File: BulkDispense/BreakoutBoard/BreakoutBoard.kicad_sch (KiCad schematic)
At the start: 0 parts

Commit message: Most Recent Changes
Added New Connector Type (3M Mini-Clamp Series)
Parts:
- added J1: Bubble Sensor Power, PartsLibrary:CONN_37204-62A3-004PL_3MM, symbol Connector:Conn_01x04_Socket
- added J10: Reagent Media Valve Signal, PartsLibrary:CONN_37204-62A3-004PL_3MM, symbol Connector:Conn_01x04_Socket
- added J11: Proportional Control Valve, PartsLibrary:CONN_37204-62A3-004PL_3MM, symbol Connector:Conn_01x04_Socket
- added J12: Reagent Media Valve GND, PartsLibrary:CONN_37204-62A3-004PL_3MM, symbol Connector:Conn_01x04_Socket
- added J13: Pressure Sensor, PartsLibrary:CONN_37204-62A3-004PL_3MM, symbol Connector:Conn_01x04_Socket
- added J14: Waste 2/2 Media Valve GND, PartsLibrary:CONN04_2165712004_MOL, symbol Connector:Conn_01x04_Socket
- added J15: Waste 2/2 Media Valve Power, PartsLibrary:CONN04_2165712004_MOL, symbol Connector:Conn_01x04_Socket
- added J16: Waste 3/2 Media Valve, PartsLibrary:CONN04_2165712004_MOL, symbol Connector:Conn_01x04_Socket
- added J17: Waste Bottle Sensor 1, PartsLibrary:CONN03_2165711003_MOL, symbol Connector:Conn_01x03_Socket
- added J18: Waste Line Sensor 2, PartsLibrary:CONN03_2165711003_MOL, symbol Connector:Conn_01x03_Socket
- added J19: Waste Line Sensor 1, PartsLibrary:CONN03_2165711003_MOL, symbol Connector:Conn_01x03_Socket
- added J2: Bubble Sensor Signal, PartsLibrary:CONN_37204-62A3-004PL_3MM, symbol Connector:Conn_01x04_Socket
- added J20: Waste Bottle Sensor 2, PartsLibrary:CONN03_2165711003_MOL, symbol Connector:Conn_01x03_Socket
- added J21: Waste Vacuum Sensor 1, PartsLibrary:CONN03_2165711003_MOL, symbol Connector:Conn_01x03_Socket
- added J22: Waste Vacuum Sensor 2, PartsLibrary:CONN03_2165711003_MOL, symbol Connector:Conn_01x03_Socket
- added J23: MAXI Power, PartsLibrary:CONN02_2165711002_MOL, symbol Connector:Conn_01x02_Socket
- added J3: Bubble Sensor GND, PartsLibrary:CONN_37204-62A3-004PL_3MM, symbol Connector:Conn_01x04_Socket
- added J33: 37212-62M3-003PL, CONN_37212-62M3-003PL_3MM, symbol 37212-62M3-003PL:37212-62M3-003PL
- added J4: Overflow Sensor Power, PartsLibrary:CONN_37204-62A3-004PL_3MM, symbol Connector:Conn_01x04_Socket
- added J5: Overflow Sensor GND, PartsLibrary:CONN_37204-62A3-004PL_3MM, symbol Connector:Conn_01x04_Socket
- added J6: Overflow Sensor Signal, PartsLibrary:CONN_37204-62A3-004PL_3MM, symbol Connector:Conn_01x04_Socket
- added J7: Power Source, PartsLibrary:691137710002, symbol Connector:Screw_Terminal_01x02
- added J8: Reagent Valve Power, PartsLibrary:CONN_37204-62A3-004PL_3MM, symbol Connector:Conn_01x04_Socket
- added J9: Reagent Valve GND, PartsLibrary:CONN_37204-62A3-004PL_3MM, symbol Connector:Conn_01x04_Socket
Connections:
- new net +24V: J1.1 (Pin_1), J1.2 (Pin_2), J1.3 (Pin_3), J1.4 (Pin_4), J11.1 (Pin_1), J13.1 (Pin_1), J15.1 (Pin_1), J15.2 (Pin_2), J15.3 (Pin_3), J15.4 (Pin_4), J16.1 (Pin_1), J16.2 (Pin_2), J17.1 (Pin_1), J18.1 (Pin_1), J19.1 (Pin_1), J20.1 (Pin_1), J21.1 (Pin_1), J22.1 (Pin_1), J23.1 (Pin_1), J33.1, J33.4, J4.1 (Pin_1), J4.2 (Pin_2), J4.3 (Pin_3), J4.4 (Pin_4), J7.1 (Pin_1), J8.1 (Pin_1), J8.2 (Pin_2), J8.3 (Pin_3), J8.4 (Pin_4)
- new net AI0: J2.4 (Pin_4)
- new net AI1: J2.3 (Pin_3)
- new net AI12: J13.4 (Pin_4)
- new net AI13: J11.2 (Pin_2)
- new net AI2: J2.2 (Pin_2)
- new net AI3: J2.1 (Pin_1)
- new net AI4: J19.3 (Pin_3), J33.3
- new net AI5: J18.3 (Pin_3), J33.5
- new net AI6: J20.3 (Pin_3), J33.6
- new net AI7: J17.3 (Pin_3), J33.7
- new net AI8: J21.3 (Pin_3), J33.8
- new net AI9: J22.3 (Pin_3), J33.9
- new net AO0: J11.3 (Pin_3)
- new net DI0: J6.4 (Pin_4)
- new net DI1: J6.3 (Pin_3)
- new net DI2: J6.2 (Pin_2)
- new net DI3: J6.1 (Pin_1)
- new net DO0: J10.4 (Pin_4)
- new net DO1: J10.3 (Pin_3)
- new net DO2: J10.2 (Pin_2)
- new net DO3: J10.1 (Pin_1)
- new net GND: J11.4 (Pin_4), J12.1 (Pin_1), J12.2 (Pin_2), J12.3 (Pin_3), J12.4 (Pin_4), J13.2 (Pin_2), J13.3 (Pin_3), J14.1 (Pin_1), J14.2 (Pin_2), J14.3 (Pin_3), J14.4 (Pin_4), J16.3 (Pin_3), J16.4 (Pin_4), J17.2 (Pin_2), J18.2 (Pin_2), J19.2 (Pin_2), J20.2 (Pin_2), J21.2 (Pin_2), J22.2 (Pin_2), J23.2 (Pin_2), J3.1 (Pin_1), J3.2 (Pin_2), J3.3 (Pin_3), J3.4 (Pin_4), J33.12, J33.2, J5.1 (Pin_1), J5.2 (Pin_2), J5.3 (Pin_3), J5.4 (Pin_4), J7.2 (Pin_2), J9.1 (Pin_1), J9.2 (Pin_2), J9.3 (Pin_3), J9.4 (Pin_4)
- no-connect marks 0 -> 2
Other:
- added sheet Controllino MAXI Expansion Board (expansion_board.kicad_sch)
- note added: "BS1"
- note added: "BS2"
- note added: "BS3"
- note added: "BS4"
- note added: "Dispense"
- note added: "MV1"
- note added: "MV2"
- note added: "MV3"
- note added: "MV4"
- note added: "OS1"
- note added: "OS2"
- note added: "OS3"
- note added: "OS4"
- note added: "Pheonix Contact"
- note added: "Power Source"
- note added: "R0"
- note added: "R1"
- note added: "R2"
- note added: "R3"
- note added: "R4"
- note added: "R5"
- note added: "R6"
- note added: "R7"
- note added: "R8"
- note added: "R9"
- note added: "Waste"

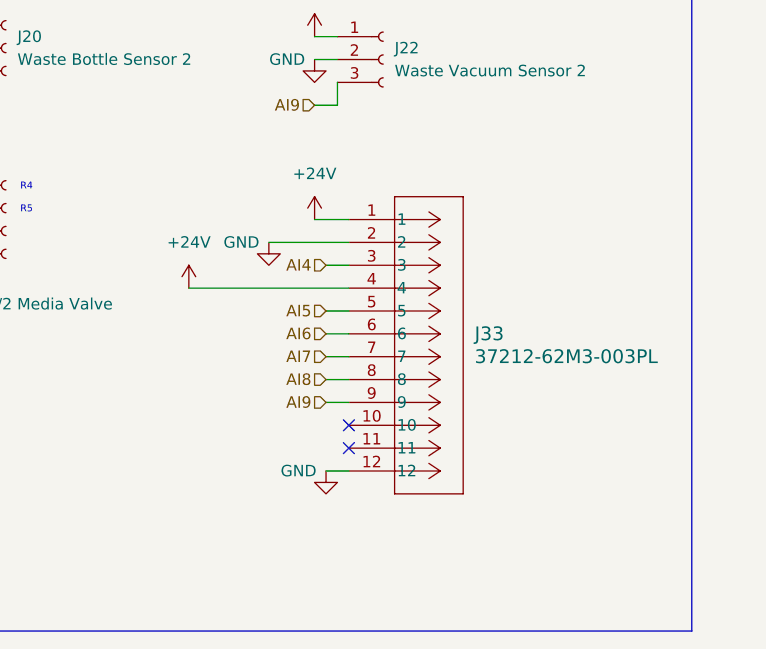
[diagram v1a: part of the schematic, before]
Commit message: Update 3POS Connectors with Mini-Clamp
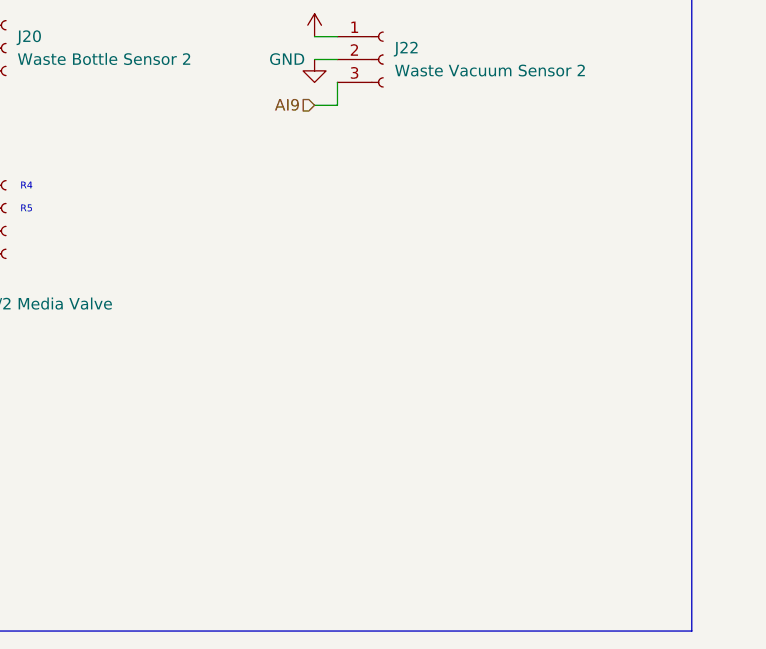
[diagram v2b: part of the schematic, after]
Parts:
- removed J33: 37212-62M3-003PL, CONN_37212-62M3-003PL_3MM, symbol 37212-62M3-003PL:37212-62M3-003PL
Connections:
- no-connect marks 2 -> 0

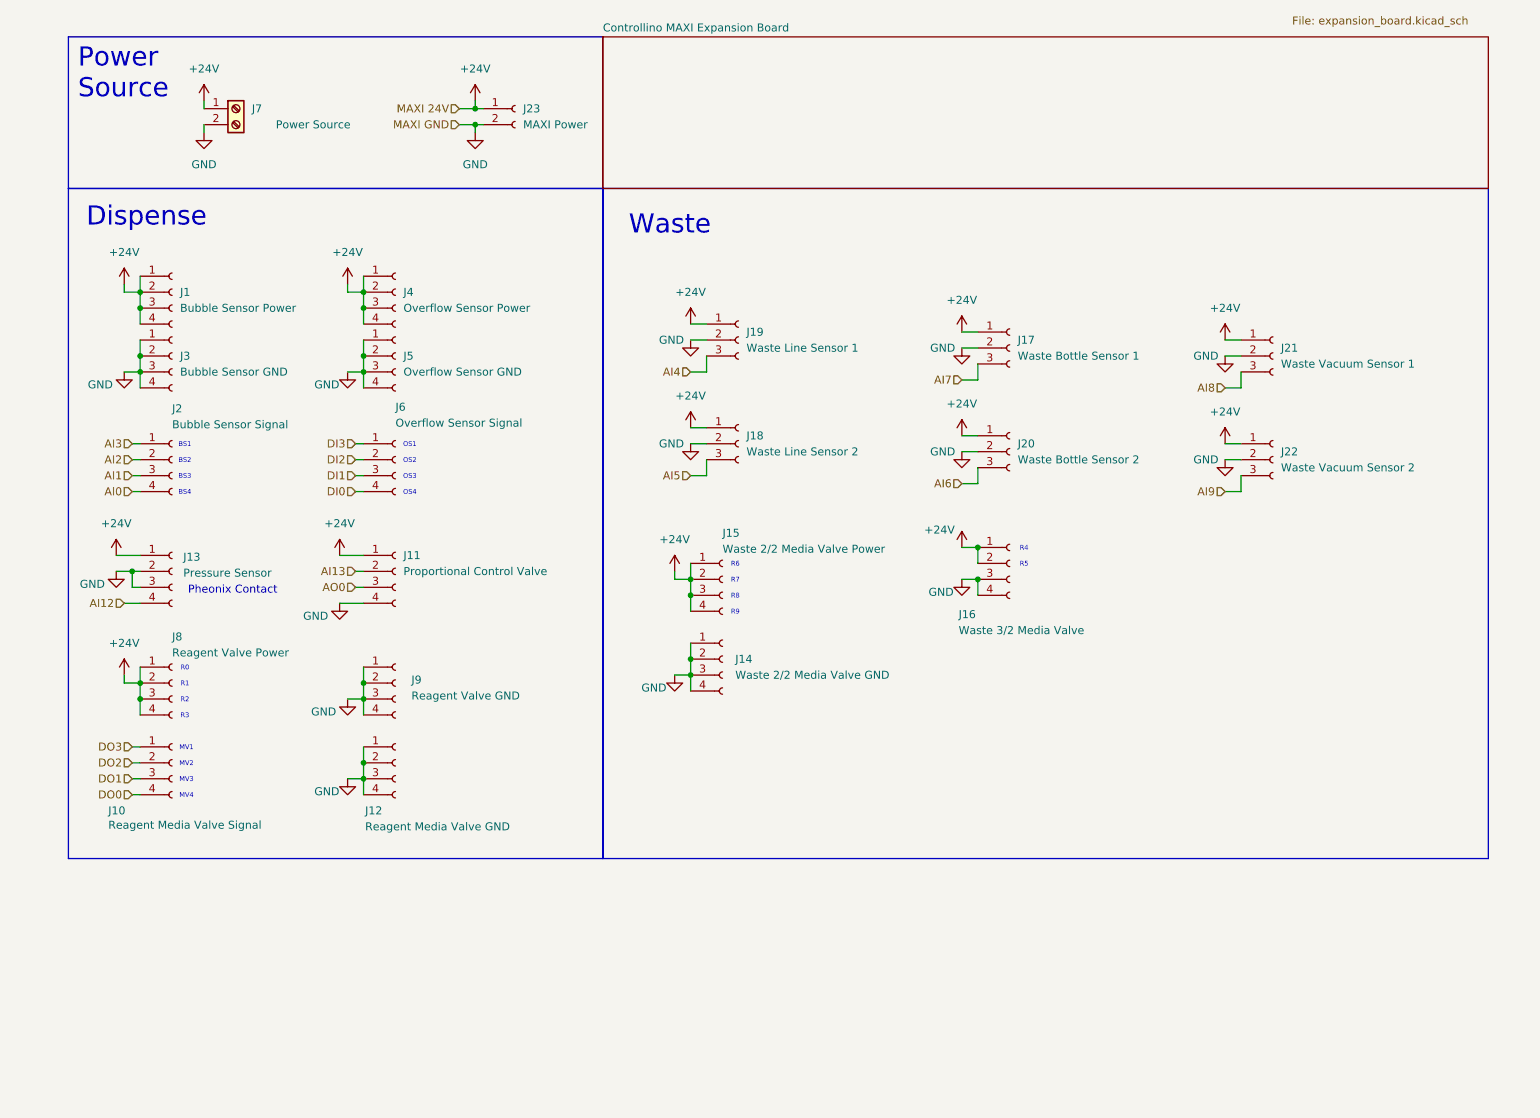
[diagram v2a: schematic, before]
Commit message: First Draft of BreakoutBoard
- Included MAXI Expansion Board Starter
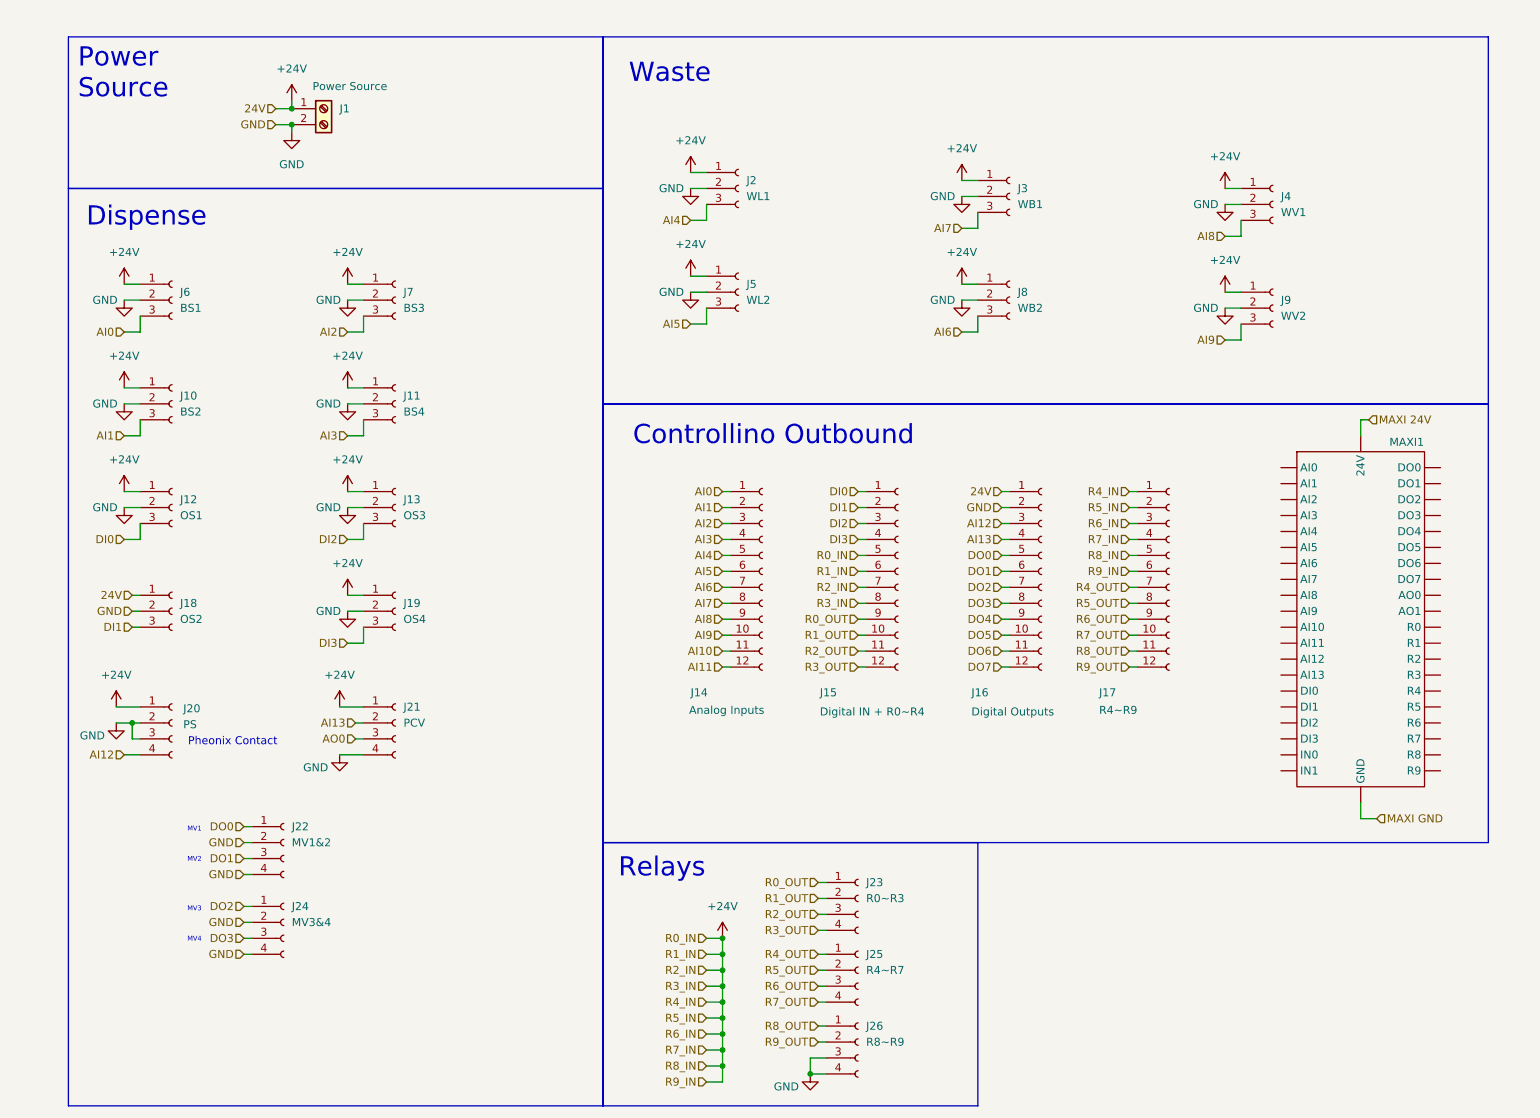
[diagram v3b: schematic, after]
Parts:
- removed J1: Bubble Sensor Power, PartsLibrary:CONN_37204-62A3-004PL_3MM, symbol Connector:Conn_01x04_Socket
- removed J10: Reagent Media Valve Signal, PartsLibrary:CONN_37204-62A3-004PL_3MM, symbol Connector:Conn_01x04_Socket
- removed J12: Reagent Media Valve GND, PartsLibrary:CONN_37204-62A3-004PL_3MM, symbol Connector:Conn_01x04_Socket
- removed J14: Waste 2/2 Media Valve GND, PartsLibrary:CONN04_2165712004_MOL, symbol Connector:Conn_01x04_Socket
- removed J15: Waste 2/2 Media Valve Power, PartsLibrary:CONN04_2165712004_MOL, symbol Connector:Conn_01x04_Socket
- removed J16: Waste 3/2 Media Valve, PartsLibrary:CONN04_2165712004_MOL, symbol Connector:Conn_01x04_Socket
- removed J2: Bubble Sensor Signal, PartsLibrary:CONN_37204-62A3-004PL_3MM, symbol Connector:Conn_01x04_Socket
- removed J23: MAXI Power, PartsLibrary:CONN02_2165711002_MOL, symbol Connector:Conn_01x02_Socket
- removed J3: Bubble Sensor GND, PartsLibrary:CONN_37204-62A3-004PL_3MM, symbol Connector:Conn_01x04_Socket
- removed J4: Overflow Sensor Power, PartsLibrary:CONN_37204-62A3-004PL_3MM, symbol Connector:Conn_01x04_Socket
- removed J5: Overflow Sensor GND, PartsLibrary:CONN_37204-62A3-004PL_3MM, symbol Connector:Conn_01x04_Socket
- removed J6: Overflow Sensor Signal, PartsLibrary:CONN_37204-62A3-004PL_3MM, symbol Connector:Conn_01x04_Socket
- removed J8: Reagent Valve Power, PartsLibrary:CONN_37204-62A3-004PL_3MM, symbol Connector:Conn_01x04_Socket
- removed J9: Reagent Valve GND, PartsLibrary:CONN_37204-62A3-004PL_3MM, symbol Connector:Conn_01x04_Socket
- added J10: BS2, PartsLibrary:3720362A3003PL, symbol Connector:Conn_01x03_Socket
- added J11: BS4, PartsLibrary:3720362A3003PL, symbol Connector:Conn_01x03_Socket
- added J12: OS1, PartsLibrary:3720362A3003PL, symbol Connector:Conn_01x03_Socket
- added J13: OS3, PartsLibrary:3720362A3003PL, symbol Connector:Conn_01x03_Socket
- added J14: Analog Inputs, PartsLibrary:CONN_37212-62M3-003PL_3MM, symbol Connector:Conn_01x12_Socket
- added J15: Digital IN + R0~R4, PartsLibrary:CONN_37212-62M3-003PL_3MM, symbol Connector:Conn_01x12_Socket
- added J16: Digital Outputs, PartsLibrary:CONN_37212-62M3-003PL_3MM, symbol Connector:Conn_01x12_Socket
- added J17: R4~R9, PartsLibrary:CONN_37212-62M3-003PL_3MM, symbol Connector:Conn_01x12_Socket
- added J18: OS2, PartsLibrary:3720362A3003PL, symbol Connector:Conn_01x03_Socket
- added J19: OS4, PartsLibrary:3720362A3003PL, symbol Connector:Conn_01x03_Socket
- added J22: MV1&2, PartsLibrary:CONN_37204-62A3-004PL_3MM, symbol Connector:Conn_01x04_Socket
- added J23: R0~R3, PartsLibrary:CONN_37204-62A3-004PL_3MM, symbol Connector:Conn_01x04_Socket
- added J24: MV3&4, PartsLibrary:CONN_37204-62A3-004PL_3MM, symbol Connector:Conn_01x04_Socket
- added J25: R4~R7, PartsLibrary:CONN_37204-62A3-004PL_3MM, symbol Connector:Conn_01x04_Socket
- added J26: R8~R9, PartsLibrary:CONN_37204-62A3-004PL_3MM, symbol Connector:Conn_01x04_Socket
- added J6: BS1, PartsLibrary:3720362A3003PL, symbol Connector:Conn_01x03_Socket
- added J7: BS3, PartsLibrary:3720362A3003PL, symbol Connector:Conn_01x03_Socket
- added MAXI1: ~, symbol SymbolLibrary:Controllino_MAXI
- J2: renamed from J19; value Waste Line Sensor 1 -> WL1; footprint PartsLibrary:CONN03_2165711003_MOL -> PartsLibrary:3720362A3003PL
- J20: renamed from J13; value Pressure Sensor -> PS
- J21: renamed from J11; value Proportional Control Valve -> PCV
- J3: renamed from J17; value Waste Bottle Sensor 1 -> WB1; footprint PartsLibrary:CONN03_2165711003_MOL -> PartsLibrary:3720362A3003PL
- J4: renamed from J21; value Waste Vacuum Sensor 1 -> WV1; footprint PartsLibrary:CONN03_2165711003_MOL -> PartsLibrary:3720362A3003PL
- J5: renamed from J18; value Waste Line Sensor 2 -> WL2; footprint PartsLibrary:CONN03_2165711003_MOL -> PartsLibrary:3720362A3003PL
- J8: renamed from J20; value Waste Bottle Sensor 2 -> WB2; footprint PartsLibrary:CONN03_2165711003_MOL -> PartsLibrary:3720362A3003PL
- J9: renamed from J22; value Waste Vacuum Sensor 2 -> WV2; footprint PartsLibrary:CONN03_2165711003_MOL -> PartsLibrary:3720362A3003PL
- renumbered J7 to J1
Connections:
- net +24V: now also J10.1 (Pin_1), J11.1 (Pin_1), J12.1 (Pin_1), J13.1 (Pin_1), J15.5 (Pin_5), J15.6 (Pin_6), J15.7 (Pin_7), J15.8 (Pin_8), J16.1 (Pin_1), J17.1 (Pin_1), J17.2 (Pin_2), J17.3 (Pin_3), J17.4 (Pin_4), J17.5 (Pin_5), J17.6 (Pin_6), J18.1 (Pin_1), J19.1 (Pin_1), J6.1 (Pin_1), J7.1 (Pin_1)
- net AI0: now also J14.1 (Pin_1), J6.3 (Pin_3)
- net AI1: now also J10.3 (Pin_3), J14.2 (Pin_2)
- net AI12: now also J16.3 (Pin_3)
- net AI13: now also J16.4 (Pin_4)
- net AI2: now also J14.3 (Pin_3), J7.3 (Pin_3)
- net AI3: now also J11.3 (Pin_3), J14.4 (Pin_4)
- net AI4: now also J14.5 (Pin_5)
- net AI5: now also J14.6 (Pin_6)
- net AI6: now also J14.7 (Pin_7)
- net AI7: now also J14.8 (Pin_8)
- net AI8: now also J14.9 (Pin_9)
- net AI9: now also J14.10 (Pin_10)
- net DI0: now also J12.3 (Pin_3), J15.1 (Pin_1)
- net DI1: now also J15.2 (Pin_2), J18.3 (Pin_3)
- net DI2: now also J13.3 (Pin_3), J15.3 (Pin_3)
- net DI3: now also J15.4 (Pin_4), J19.3 (Pin_3)
- net DO0: now also J16.5 (Pin_5), J22.1 (Pin_1)
- net DO1: now also J16.6 (Pin_6), J22.3 (Pin_3)
- net DO2: now also J16.7 (Pin_7), J24.1 (Pin_1)
- net DO3: now also J16.8 (Pin_8), J24.3 (Pin_3)
- net GND: now also J10.2 (Pin_2), J11.2 (Pin_2), J12.2 (Pin_2), J13.2 (Pin_2), J16.2 (Pin_2), J18.2 (Pin_2), J19.2 (Pin_2), J22.2 (Pin_2), J22.4 (Pin_4), J24.2 (Pin_2), J24.4 (Pin_4), J26.3 (Pin_3), J26.4 (Pin_4), J6.2 (Pin_2), J7.2 (Pin_2)
- new net AI10: J14.11 (Pin_11)
- new net AI11: J14.12 (Pin_12)
- new net DO4: J16.9 (Pin_9)
- new net DO5: J16.10 (Pin_10)
- new net DO6: J16.11 (Pin_11)
- new net DO7: J16.12 (Pin_12)
- new net MAXI 24V: MAXI1. (R9)
- new net MAXI GND: MAXI1. (R9)
- new net R0_OUT: J15.9 (Pin_9), J23.1 (Pin_1)
- new net R1_OUT: J15.10 (Pin_10), J23.2 (Pin_2)
- new net R2_OUT: J15.11 (Pin_11), J23.3 (Pin_3)
- new net R3_OUT: J15.12 (Pin_12), J23.4 (Pin_4)
- new net R4_OUT: J17.7 (Pin_7), J25.1 (Pin_1)
- new net R5_OUT: J17.8 (Pin_8), J25.2 (Pin_2)
- new net R6_OUT: J17.9 (Pin_9), J25.3 (Pin_3)
- new net R7_OUT: J17.10 (Pin_10), J25.4 (Pin_4)
- new net R8_OUT: J17.11 (Pin_11), J26.1 (Pin_1)
- new net R9_OUT: J17.12 (Pin_12), J26.2 (Pin_2)
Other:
- removed sheet Controllino MAXI Expansion Board
- note added: "Controllino Outbound"
- note added: "Relays"
- note removed: "BS1"
- note removed: "BS2"
- note removed: "BS3"
- note removed: "BS4"
- note removed: "OS1"
- note removed: "OS2"
- note removed: "OS3"
- note removed: "OS4"
- note removed: "R0"
- note removed: "R1"
- note removed: "R2"
- note removed: "R3"
- note removed: "R4"
- note removed: "R5"
- note removed: "R6"
- note removed: "R7"
- note removed: "R8"
- note removed: "R9"
- moved on the sheet: J1, J2, J20, J21, J3, J4, J5, J8, J9

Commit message: Add more documentation + holding mounts
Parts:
- added H1, H2, H3, H4: MountingHole, MountingHole:MountingHole_2.2mm_M2, symbol Mechanical:MountingHole
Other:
- company: (none) -> Moderna
- title: (none) -> Bulk Dispenser Breakout Board
- moved on the sheet: J10, J11, J12, J13, J18, J19, J20, J21, J22, J24, J4, J6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

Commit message: Finished Up Board + MAXIExpansionBoard
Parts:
- removed J1: Power Source, PartsLibrary:691137710002, symbol Connector:Screw_Terminal_01x02
- added J12: FS1, PartsLibrary:CONN_37204-62A3-004PL_3MM, symbol Connector:Conn_01x04_Socket
- added J13: FS3, PartsLibrary:CONN_37204-62A3-004PL_3MM, symbol Connector:Conn_01x04_Socket
- added J15: FS2, PartsLibrary:CONN_37204-62A3-004PL_3MM, symbol Connector:Conn_01x04_Socket
- added J16: FS4, PartsLibrary:CONN_37204-62A3-004PL_3MM, symbol Connector:Conn_01x04_Socket
- added J30: Flow Sensors, PartsLibrary:CONN_37212-62M3-003PL_3MM, symbol Connector:Conn_01x12_Socket
- renumbered J6 to J1, J13 to J10, J19 to J11, J21 to J14, J2 to J17, J5 to J18, J14 to J19, J10 to J2, J23 to J20, J25 to J21, J26 to J22, J15 to J23, J3 to J24, J8 to J25, J16 to J26, J17 to J27, J4 to J28, J9 to J29, J12 to J3, J18 to J4, J20 to J5, J22 to J6, J24 to J7, J7 to J8, J11 to J9
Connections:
- net AI4: now also J24.3 (Pin_3); no longer J17.3 (Pin_3)
- net AI5: now also J25.3 (Pin_3); no longer J18.3 (Pin_3)
- net AI6: now also J17.3 (Pin_3); no longer J25.3 (Pin_3)
- net AI7: now also J18.3 (Pin_3); no longer J24.3 (Pin_3)
- net AO0: now also J30.11 (Pin_11)
- net AI10 renamed FS1-1
- net FS1-1: now also J12.1 (Pin_1)
- net AI11 renamed FS1-2
- net FS1-2: now also J12.2 (Pin_2)
- net DO4 renamed FS1-3
- net FS1-3: now also J12.3 (Pin_3)
- net DO5 renamed FS1-4
- net FS1-4: now also J12.4 (Pin_4)
- net DO6 renamed FS2-1
- net FS2-1: now also J15.1 (Pin_1)
- net DO7 renamed FS2-2
- net FS2-2: now also J15.2 (Pin_2)
- new net FS2-3: J15.3 (Pin_3), J30.1 (Pin_1)
- new net FS2-4: J15.4 (Pin_4), J30.2 (Pin_2)
- new net FS3-1: J13.1 (Pin_1), J30.3 (Pin_3)
- new net FS3-2: J13.2 (Pin_2), J30.4 (Pin_4)
- new net FS3-3: J13.3 (Pin_3), J30.5 (Pin_5)
- new net FS3-4: J13.4 (Pin_4), J30.6 (Pin_6)
- new net FS4-1: J16.1 (Pin_1), J30.7 (Pin_7)
- new net FS4-2: J16.2 (Pin_2), J30.8 (Pin_8)
- new net FS4-3: J16.3 (Pin_3), J30.9 (Pin_9)
- new net FS4-4: J16.4 (Pin_4), J30.10 (Pin_10)
- no-connect marks 0 -> 1
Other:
- moved on the sheet: J19, J23, J26, J27
